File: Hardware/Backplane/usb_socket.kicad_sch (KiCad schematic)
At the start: 7 parts, among them J2102 USB_A

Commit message: Some cleanups of Backplane schematic: Adds DigiKey part numbers, removes unnecessary properties, marks test points as excluded from BOM
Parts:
- TP2103, TP2104, TP2105: now left out of the parts list
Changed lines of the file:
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@@
 			)
 		)
-		(property "Datasheet" "~"
+		(property "Datasheet" ""
 			(at 83.82 74.295 0)
 			(effects
@@
 			)
 		)
-		(property "Datasheet" "~"
+		(property "Datasheet" ""
 			(at 77.47 60.325 0)
 			(effects
@@
 		(unit 1)
 		(exclude_from_sim no)
-		(in_bom yes)
+		(in_bom no)
 		(on_board yes)
 		(dnp no)
@@
 		(unit 1)
 		(exclude_from_sim no)
-		(in_bom yes)
+		(in_bom no)
 		(on_board yes)
 		(dnp no)
@@
 		(unit 1)
 		(exclude_from_sim no)
-		(in_bom yes)
+		(in_bom no)
 		(on_board yes)
 		(dnp no)
@@
 			)
 		)
-		(property "Datasheet" "~"
+		(property "Datasheet" ""
 			(at 86.36 74.295 0)
 			(effects

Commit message: Adjusts to review comments
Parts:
- F2101: footprint (none) -> Fuse:Fuse_1206_3216Metric; Digikey Part No (none) -> 13-SMD1206B050TF/15TR-ND
- R2102, R2103: Digikey Part No (none) -> 311-0.0GRCT-ND
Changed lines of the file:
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@@
 			)
 		)
-		(property "Datasheet" ""
+		(property "Datasheet" "https://www.yageogroup.com/content/datasheet/asset/file/PYU-RC_GROUP_51_ROHS_L"
 			(at 83.82 74.295 0)
 			(effects
@@
 		(property "Description" "Resistor, small symbol"
 			(at 83.82 74.295 0)
+			(effects
+				(font
+					(size 1.27 1.27)
+				)
+				(hide yes)
+			)
+		)
+		(property "Digikey Part No" "311-0.0GRCT-ND"
+			(at 83.82 74.295 90)
 			(effects
 				(font
@@
 			)
 		)
-		(property "Datasheet" ""
+		(property "Datasheet" "https://www.yageogroup.com/content/datasheet/asset/file/PYU-RC_GROUP_51_ROHS_L"
 			(at 86.36 74.295 0)
 			(effects
@@
 		(property "Description" "Resistor, small symbol"
 			(at 86.36 74.295 0)
+			(effects
+				(font
+					(size 1.27 1.27)
+				)
+				(hide yes)
+			)
+		)
+		(property "Digikey Part No" "311-0.0GRCT-ND"
+			(at 86.36 74.295 90)
 			(effects
 				(font
@@
 			)
 		)
-		(property "Footprint" ""
+		(property "Footprint" "Fuse:Fuse_1206_3216Metric"
 			(at 57.15 53.975 0)
 			(effects
@@
 					(size 1.27 1.27)
 				)
-			)
-		)
-		(property "Datasheet" ""
+				(hide yes)
+			)
+		)
+		(property "Datasheet" "https://www.yageogroup.com/content/Resource%20Library/Datasheet/SMD1206_1.pdf"
 			(at 57.15 53.975 0)
 			(effects
@@
 					(size 1.27 1.27)
 				)
+				(hide yes)
 			)
 		)
@@
 					(size 1.27 1.27)
 				)
-			)
-		)
+				(hide yes)
+			)
+		)
+		(property "Digikey Part No" "13-SMD1206B050TF/15TR-ND"
+			(at 57.15 53.975 90)
+			(effects
+				(font
+					(size 1.27 1.27)
+				)
+				(hide yes)
+			)
+		)

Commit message: Cleans up schematic even more, consolidates 270 and 100 Ohm resistors into the 560 ohm resistor, as they were only used as series resistors for the mosfets and LED current limiters
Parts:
- J2102: footprint (none) -> Connector_USB:USB_A_Receptacle_GCT_USB1046; Digikey Part No (none) -> 2073-USB1046-GF-0190-L-B-ACT-ND
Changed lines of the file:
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@@
 			)
 		)
-		(property "Footprint" ""
+		(property "Footprint" "Connector_USB:USB_A_Receptacle_GCT_USB1046"
 			(at 77.47 60.325 0)
 			(effects
@@
 			)
 		)
-		(property "Datasheet" ""
+		(property "Datasheet" "https://gct.co/files/specs/usb1046-spec.pdf"
 			(at 77.47 60.325 0)
 			(effects
@@
 			(at 81.28 59.055 0)
 			(effects
+				(font
+					(size 1.27 1.27)
+				)
+				(hide yes)
+			)
+		)
+		(property "Digikey Part No" "2073-USB1046-GF-0190-L-B-ACT-ND"
+			(at 81.28 59.055 0)
+			(effects

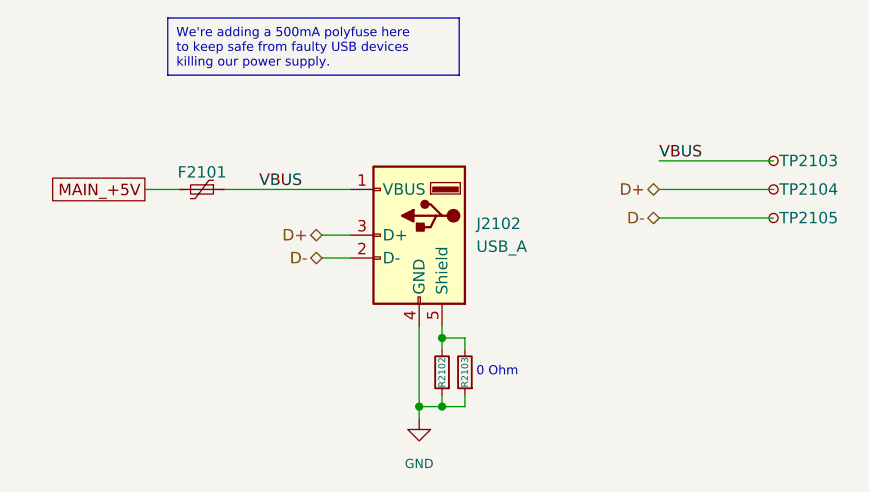
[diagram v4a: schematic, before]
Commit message: More BOM consolidation
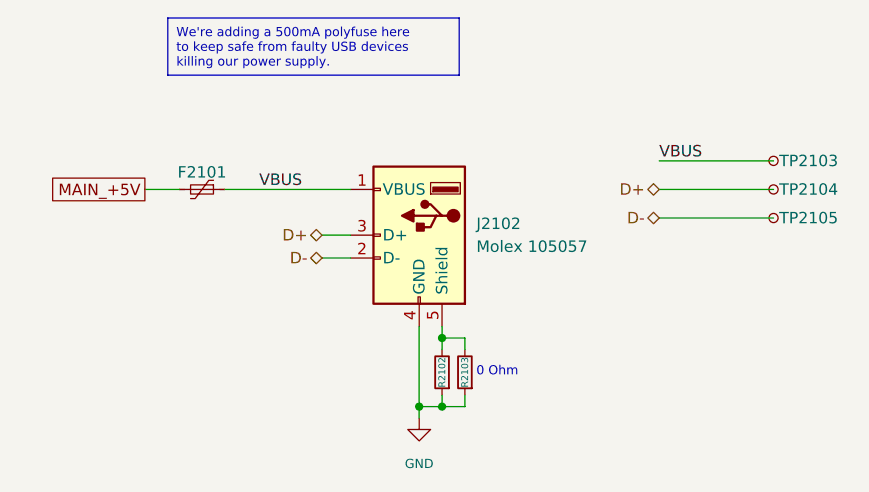
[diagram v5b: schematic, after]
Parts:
- J2102: value USB_A -> Molex 105057; footprint Connector_USB:USB_A_Receptacle_GCT_USB1046 -> Connector_USB:USB_A_Molex_105057_Vertical; Digikey Part No 2073-USB1046-GF-0190-L-B-ACT-ND -> WM8672-ND
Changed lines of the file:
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@@
 			)
 		)
-		(property "Value" "USB_A"
+		(property "Value" "Molex 105057"
 			(at 87.63 60.3249 0)
 			(effects
@@
 			)
 		)
-		(property "Footprint" "Connector_USB:USB_A_Receptacle_GCT_USB1046"
+		(property "Footprint" "Connector_USB:USB_A_Molex_105057_Vertical"
 			(at 77.47 60.325 0)
 			(effects
@@
 			)
 		)
-		(property "Datasheet" "https://gct.co/files/specs/usb1046-spec.pdf"
+		(property "Datasheet" "https://www.molex.com/pdm_docs/ps/PS-105057-001.pdf"
 			(at 77.47 60.325 0)
 			(effects
@@
 			)
 		)
-		(property "Description" "USB Type A connector"
+		(property "Description" "USB-A (USB TYPE-A) USB 2.0 Receptacle Connector 4 Position Through Hole"
 			(at 81.28 59.055 0)
 			(effects
@@
 			)
 		)
-		(property "Digikey Part No" "2073-USB1046-GF-0190-L-B-ACT-ND"
+		(property "Digikey Part No" "WM8672-ND"
 			(at 81.28 59.055 0)
 			(effects
